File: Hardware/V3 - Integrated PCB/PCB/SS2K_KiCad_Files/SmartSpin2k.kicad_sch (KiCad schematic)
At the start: 81 parts, among them J1 B4B-XH-AMLFSN, J2 B4B-XH-AMLFSN, J3 B8B-XH-A_LFSN, J4 10118194-0001LF, Q1 S8050, Q2 S8050, SW1 SW_Push, SW2 SW_Push, U1 ESP32-WROOM-32D, U2 TMC2209-LA-T, U3 MAX3232, U4 TPS5430DDA, U5 INTERFACE-CP2102-GMR(QFN28), U6 LM1117-3.3

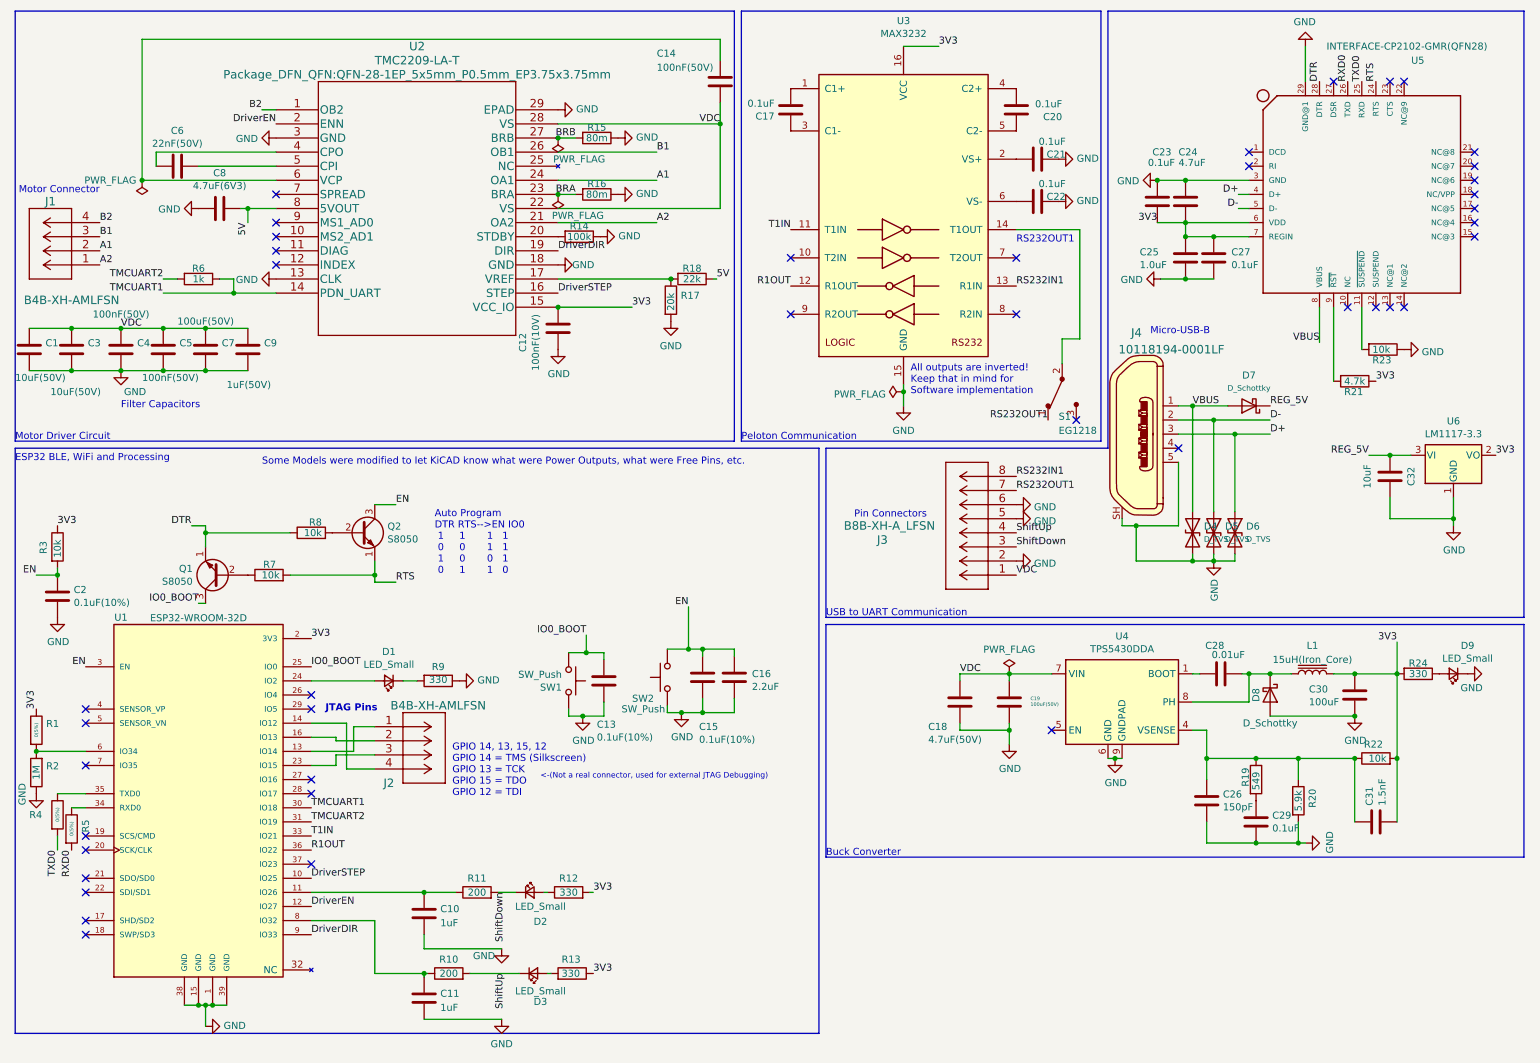
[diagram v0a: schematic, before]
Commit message: Fixed Transistor Footprint, Added new Switch, Chamfered corners
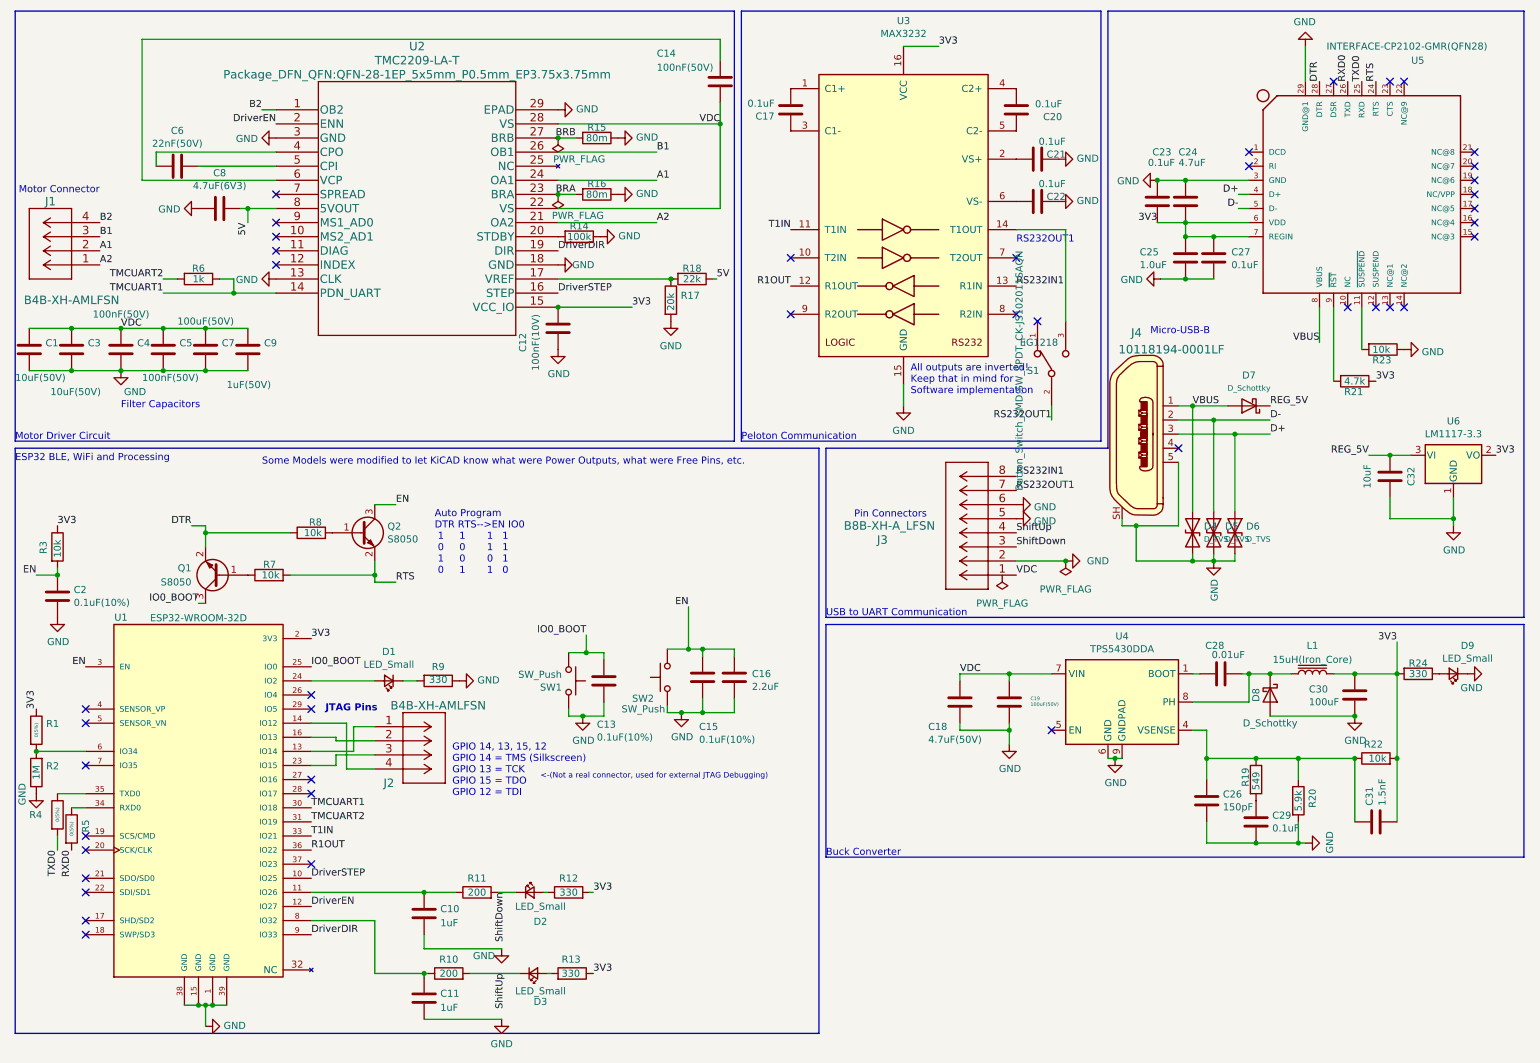
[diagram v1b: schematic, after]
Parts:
- Q1, Q2: symbol Transistor_BJT:2N2219 -> Transistor_BJT:S8050_-_SOT23
- S1: footprint Button_Switch_SMD:SW_SPDT_PCM12 -> Button_Switch_SMD:SW_SPDT_CK-JS102011SAQN; symbol dk_Slide-Switches:EG1218 -> JS102011:JS102011SAQN; Category Switches -> (none); DK_Datasheet_Link http://spec_sheets.e-switch.com/specs/P040040.pdf -> (none); DK_Detail_Page /product-detail/en/e-switch/EG1218/EG1903-ND/101726 -> (none); Digi-Key_PN EG1903-ND -> (none); Family Slide Switches -> (none); MANUFACTURER (none) -> C&K; MPN EG1218 -> (none); Manufacturer E-Switch -> (none); Status Active -> (none)
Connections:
- net DTR: now also Q1.2 (E); no longer Q1.1 (E)
- net RS232OUT1: now also S1.2; no longer S1.1
- net RTS: now also Q2.2 (E); no longer Q2.1 (E)
- net at R7.1: now also Q1.1 (B); no longer Q1.2 (B)
- net at R8.2: now also Q2.1 (B); no longer Q2.2 (B)
- net at U3.14 (T1OUT): now also S1.3; no longer S1.2

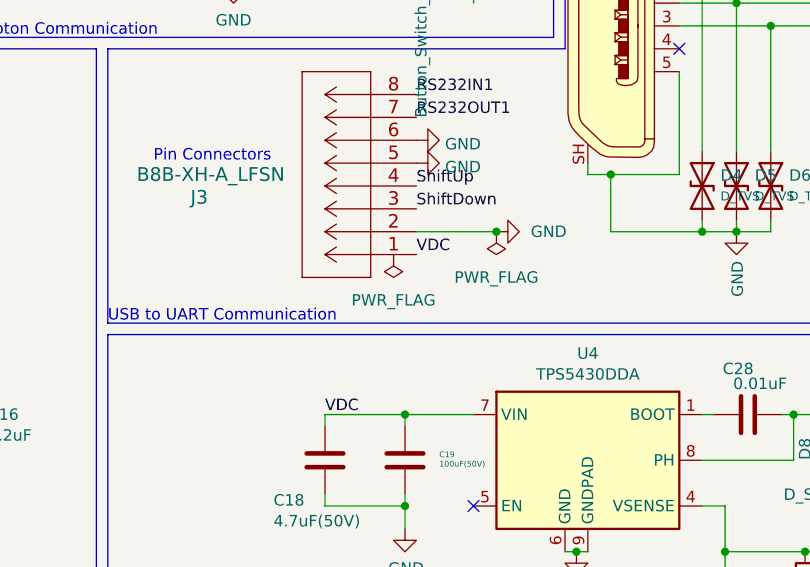
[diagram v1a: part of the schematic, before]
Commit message: Updated build files and .step for CAD
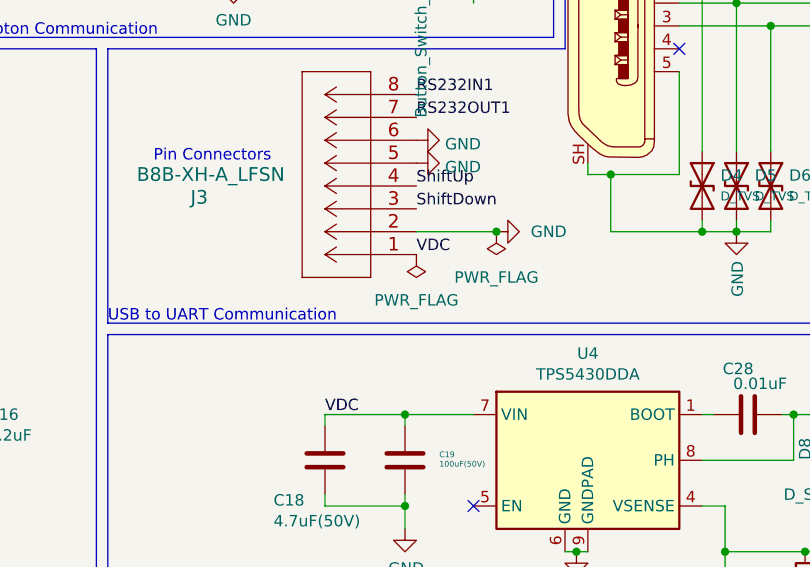
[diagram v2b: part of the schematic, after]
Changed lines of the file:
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@@
     (pin "2")
   )
-  (symbol (lib_id "power:PWR_FLAG") (at 190.5 114.3 180) (unit 1)
+  (symbol (lib_id "power:PWR_FLAG") (at 193.04 114.3 180) (unit 1)
     (in_bom yes) (on_board yes) (fields_autoplaced)
-    (property "Reference" "#FLG0101" (id 0) (at 190.5 116.205 0)
+    (property "Reference" "#FLG0101" (id 0) (at 193.04 116.205 0)
       (effects (font (size 1.27 1.27)) hide)
     )
-    (property "Value" "PWR_FLAG" (id 1) (at 190.5 119.38 0))
-    (property "Footprint" "" (id 2) (at 190.5 114.3 0)
+    (property "Value" "PWR_FLAG" (id 1) (at 193.04 119.38 0))
+    (property "Footprint" "" (id 2) (at 193.04 114.3 0)
       (effects (font (size 1.27 1.27)) hide)
     )
-    (property "Datasheet" "~" (id 3) (at 190.5 114.3 0)
+    (property "Datasheet" "~" (id 3) (at 193.04 114.3 0)
       (effects (font (size 1.27 1.27)) hide)
     )

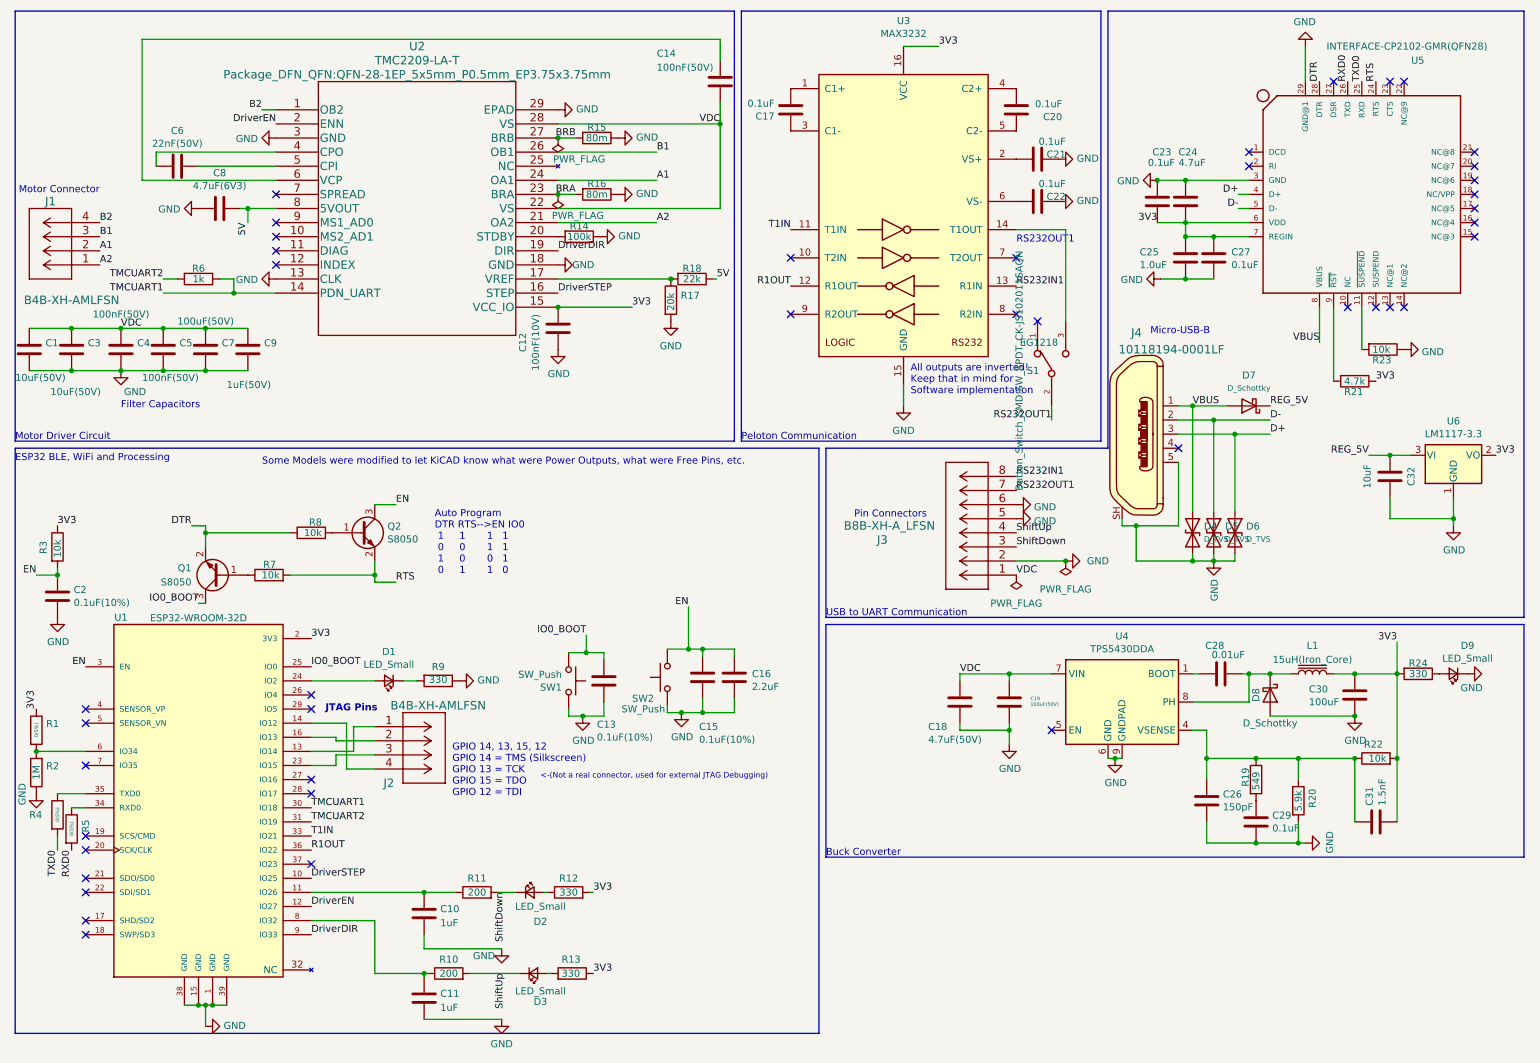
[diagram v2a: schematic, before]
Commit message: Updated PCB
Moved Switch Back
Switched A1 & A2 on Motor Jumper
Rotated back Silkscreen images
Added Silkscreen to Jumpers on back
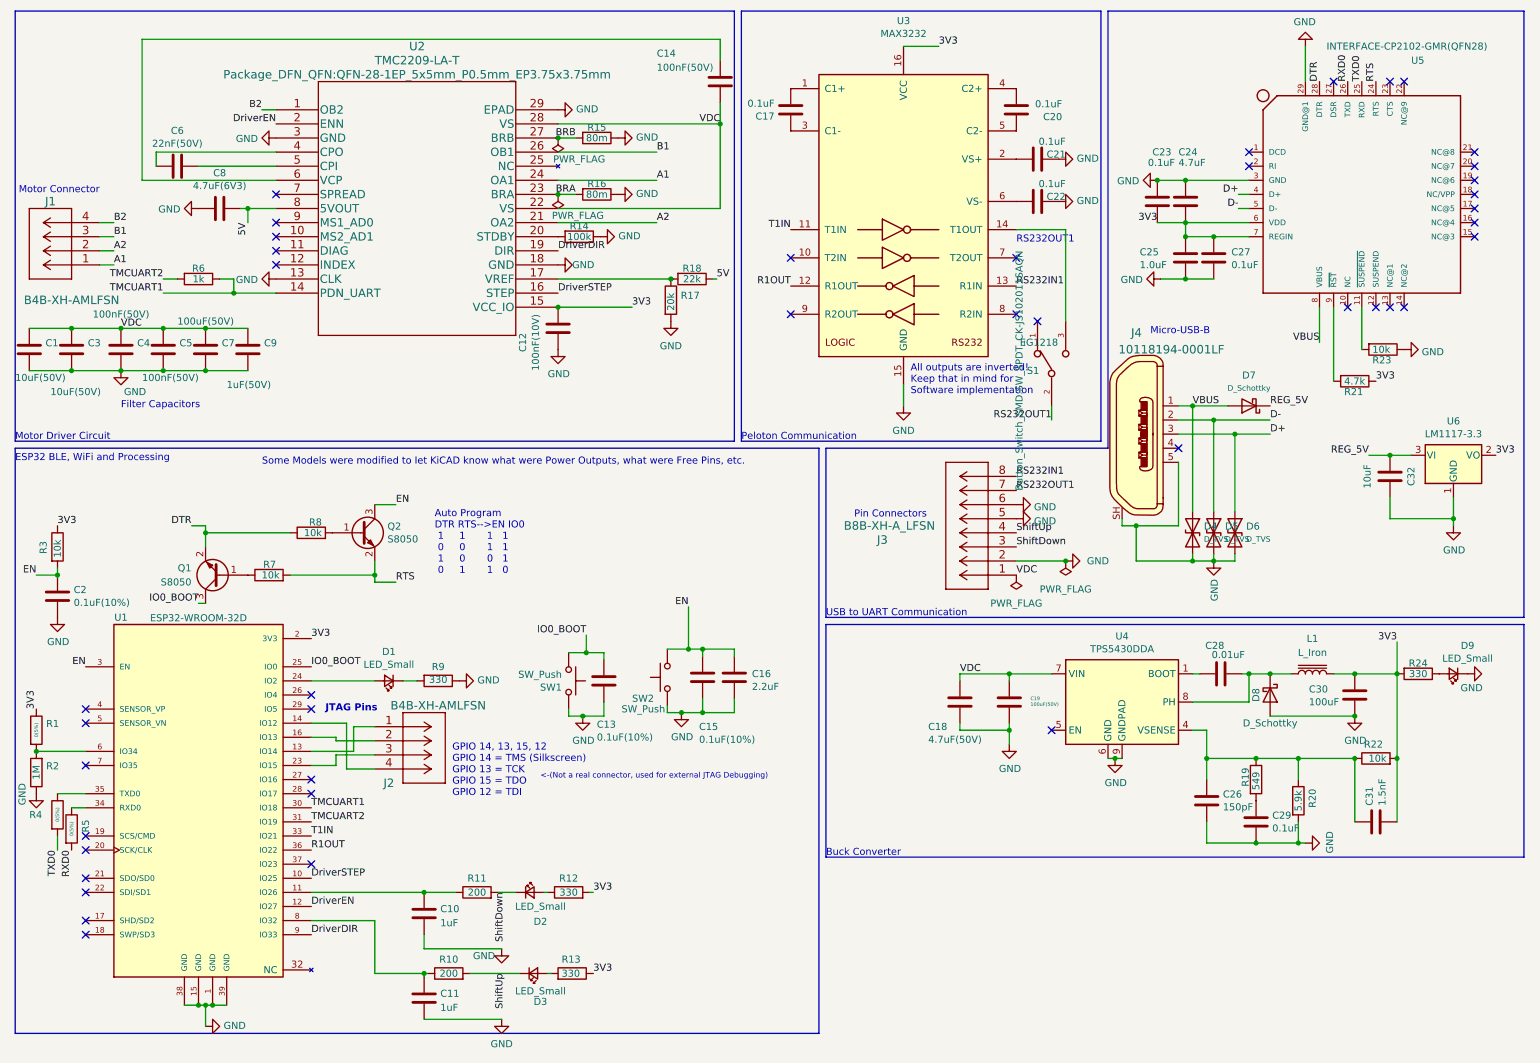
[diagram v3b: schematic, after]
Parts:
- L1: value 15uH(Iron_Core) -> L_Iron; footprint Inductor_SMD_Extra:L_SXN_SMDRI127_150MT -> Inductor_SMD:L_12x12mm_H8mm
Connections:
- net A1: now also J1.1; no longer J1.2
- net A2: now also J1.2; no longer J1.1
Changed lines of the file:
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@@
+    (stroke (width 0) (type default) (color 0 0 0 0))
+  )
+  (wire (pts (xy 30.48 58.42) (xy 27.94 58.42))
     (stroke (width 0) (type default) (color 0 0 0 0))
   )
@@
     (stroke (width 0) (type default) (color 0 0 0 0))
   )
+  (wire (pts (xy 30.48 50.8) (xy 27.94 50.8))
+    (stroke (width 0) (type default) (color 0 0 0 0))
+  )
   (wire (pts (xy 62.23 114.3) (xy 77.47 114.3))
     (stroke (width 0) (type default) (color 0 0 0 0))
@@
     (stroke (width 0) (type default) (color 0 0 0 0))
   )
+  (wire (pts (xy 30.48 55.88) (xy 27.94 55.88))
+    (stroke (width 0) (type default) (color 0 0 0 0))
+  )
   (wire (pts (xy 231.14 83.82) (xy 224.79 83.82))
     (stroke (width 0) (type default) (color 0 0 0 0))
@@
   )
   (wire (pts (xy 254 132.08) (xy 261.62 132.08))
+    (stroke (width 0) (type default) (color 0 0 0 0))
+  )
+  (wire (pts (xy 30.48 53.34) (xy 27.94 53.34))
     (stroke (width 0) (type default) (color 0 0 0 0))
   )
@@
     (effects (font (size 1.27 1.27)) (justify left bottom))
   )
-  (label "B1" (at 27.94 53.34 0)
+  (label "B1" (at 30.48 53.34 0)
     (effects (font (size 1.27 1.27)) (justify left bottom))
   )
@@
     (effects (font (size 1.27 1.27)) (justify left bottom))
   )
-  (label "B2" (at 27.94 50.8 0)
+  (label "B2" (at 30.48 50.8 0)
     (effects (font (size 1.27 1.27)) (justify left bottom))
   )
@@
     (effects (font (size 1.27 1.27)) (justify right bottom))
   )
-  (label "A1" (at 27.94 55.88 0)
+  (label "A2" (at 30.48 55.88 0)
     (effects (font (size 1.27 1.27)) (justify left bottom))
   )
@@
     (effects (font (size 1.27 1.27)) (justify right bottom))
   )
-  (label "A2" (at 27.94 58.42 0)
+  (label "A1" (at 30.48 58.42 0)
     (effects (font (size 1.27 1.27)) (justify left bottom))
   )
@@
   (symbol (lib_id "Device:L_Iron") (at 246.38 132.08 90) (unit 1)
     (in_bom yes) (on_board yes) (fields_autoplaced)
-    (property "Reference" "L1" (id 0) (at 246.38 126.9832 90))
-    (property "Value" "15uH(Iron_Core)" (id 1) (at 246.38 129.5201 90))
-    (property "Footprint" "Inductor_SMD_Extra:L_SXN_SMDRI127_150MT" (id 2) (at 246.38 132.08 0)
-      (effects (font (size 1.27 1.27)) hide)
-    )
-    (property "Datasheet" "~" (id 3) (at 246.38 132.08 0)
+    (property "Reference" "L1" (id 0) (at 246.38 125.73 90))
+    (property "Value" "L_Iron" (id 1) (at 246.38 128.27 90))
+    (property "Footprint" "Inductor_SMD:L_12x12mm_H8mm" (id 2) (at 246.38 132.08 0)
+      (effects (font (size 1.27 1.27)) hide)
+    )
+    (property "Datasheet" "https://datasheet.lcsc.com/lcsc/1811012006_Sunltech-Tech-SLH1207S150MTT_C182183.pdf" (id 3) (at 246.38 132.08 0)
       (effects (font (size 1.27 1.27)) hide)
     )
@@
     )
     (path "/13337490-c2c5-44a4-8bfb-f55df5a0d968"
-      (reference "L1") (unit 1) (value "15uH(Iron_Core)") (footprint "Inductor_SMD_Extra:L_SXN_SMDRI127_150MT")
+      (reference "L1") (unit 1) (value "L_Iron") (footprint "Inductor_SMD:L_12x12mm_H8mm")
     )
     (path "/00000000-0000-0000-0000-00006366bbe5"
